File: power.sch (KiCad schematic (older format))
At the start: 28 parts, among them J1 TYPE-C-31-M-12, U4 BQ27441DRZR-G1A, U5 MCP73831-2-OT, U6 LC05111C02MTTTG, U7 TLV75733PDBV

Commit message: Did stuff
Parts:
- C5, C6, C7: footprint (none) -> Capacitor_SMD:C_0603_1608Metric_Pad1.05x0.95mm_HandSolder
- R16, R17: footprint (none) -> Resistor_SMD:R_0603_1608Metric_Pad1.05x0.95mm_HandSolder
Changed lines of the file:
@@
 	2675 3250 2375 3250
 Wire Wire Line
-	2675 3300 2675 3250
+	4075 3300 4075 3250
 $Comp
 L power:GND #PWR?
 U 1 1 5F83C52A
-P 2675 3300
+P 4075 3300
 AR Path="/5E707A75/5F83C52A" Ref="#PWR?"  Part="1"
 AR Path="/5F83C52A" Ref="#PWR?"  Part="1"
 AR Path="/5F797DCE/5F83C52A" Ref="#PWR09"  Part="1"
-F 0 "#PWR09" H 2675 3050 50  0001 C CNN
-F 1 "GND" H 2680 3127 50  0000 C CNN
-F 2 "" H 2675 3300 50  0001 C CNN
-F 3 "" H 2675 3300 50  0001 C CNN
-	1    2675 3300
+F 0 "#PWR09" H 4075 3050 50  0001 C CNN
+F 1 "GND" H 4080 3127 50  0000 C CNN
+F 2 "" H 4075 3300 50  0001 C CNN
+F 3 "" H 4075 3300 50  0001 C CNN
+	1    4075 3300
 	1    0    0    -1
 $EndComp
@@
 F 0 "R17" H 4234 4521 50  0000 L CNN
 F 1 "1K" H 4234 4430 50  0000 L CNN
-F 2 "" H 4175 4475 50  0001 C CNN
+F 2 "Resistor_SMD:R_0603_1608Metric_Pad1.05x0.95mm_HandSolder" H 4175 4475 50  0001 C CNN
 F 3 "~" H 4175 4475 50  0001 C CNN
 	1    4175 4475
@@
 F 0 "R16" H 3617 3954 50  0000 R CNN
 F 1 "680R" H 3617 4045 50  0000 R CNN
-F 2 "" H 3675 4000 50  0001 C CNN
+F 2 "Resistor_SMD:R_0603_1608Metric_Pad1.05x0.95mm_HandSolder" H 3675 4000 50  0001 C CNN
 F 3 "~" H 3675 4000 50  0001 C CNN
 	1    3675 4000
@@
 F 0 "C6" H 2875 4325 50  0000 R CNN
 F 1 "100nF" H 3000 4425 50  0000 R CNN
-F 2 "" H 2750 4525 50  0001 C CNN
+F 2 "Capacitor_SMD:C_0603_1608Metric_Pad1.05x0.95mm_HandSolder" H 2750 4525 50  0001 C CNN
 F 3 "~" H 2750 4525 50  0001 C CNN
 	1    2750 4525
@@
 F 0 "C7" H 3025 4600 50  0000 R CNN
 F 1 "100nF" H 3050 4675 50  0000 R CNN
-F 2 "" H 3075 4525 50  0001 C CNN
+F 2 "Capacitor_SMD:C_0603_1608Metric_Pad1.05x0.95mm_HandSolder" H 3075 4525 50  0001 C CNN
 F 3 "~" H 3075 4525 50  0001 C CNN
 	1    3075 4525
@@
 F 0 "C5" H 4375 4475 50  0000 R CNN
 F 1 "100nF" H 4450 4550 50  0000 R CNN
-F 2 "" H 4450 4450 50  0001 C CNN
+F 2 "Capacitor_SMD:C_0603_1608Metric_Pad1.05x0.95mm_HandSolder" H 4450 4450 50  0001 C CNN
 F 3 "~" H 4450 4450 50  0001 C CNN
 	1    4450 4450
@@
 Replace with LM66100
 Wire Notes Line
-	5725 3900 5625 3900
-Wire Notes Line
-	5625 3900 5625 4100
-Wire Notes Line
-	5625 4100 5725 4100
+	5375 3900 5375 4100
+Wire Notes Line
+	5375 4100 5725 4100
 Wire Notes Line
 	5725 4100 5725 3825
 Wire Notes Line
 	5725 3825 6575 3825
+Wire Notes Line
+	5375 3900 5725 3900
 $EndSCHEMATC

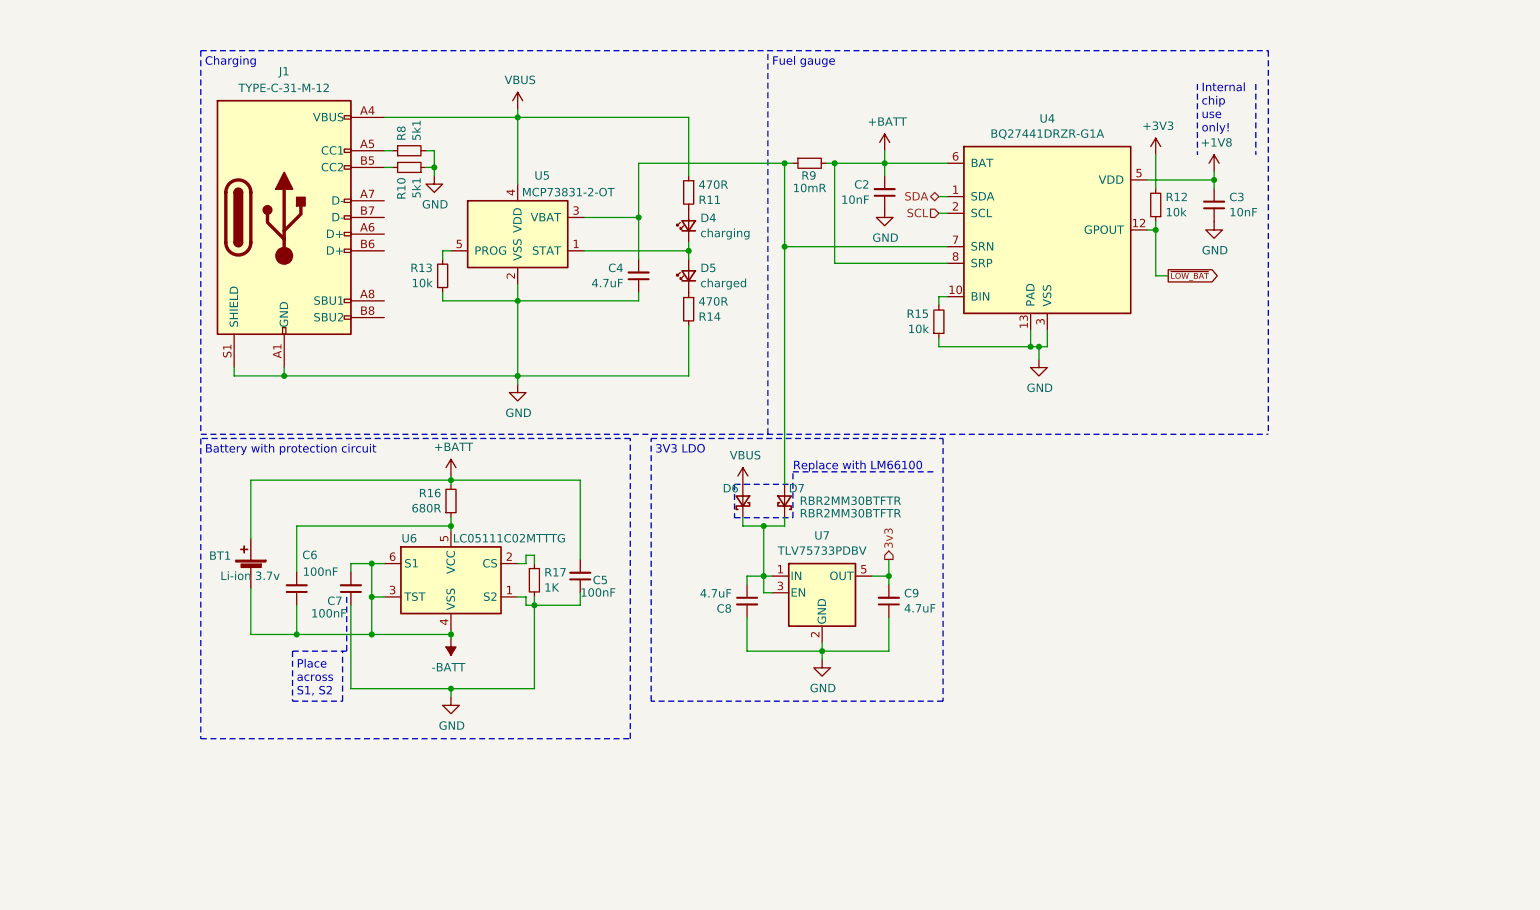
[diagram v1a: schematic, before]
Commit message: Redesigned to small-stick formfactor
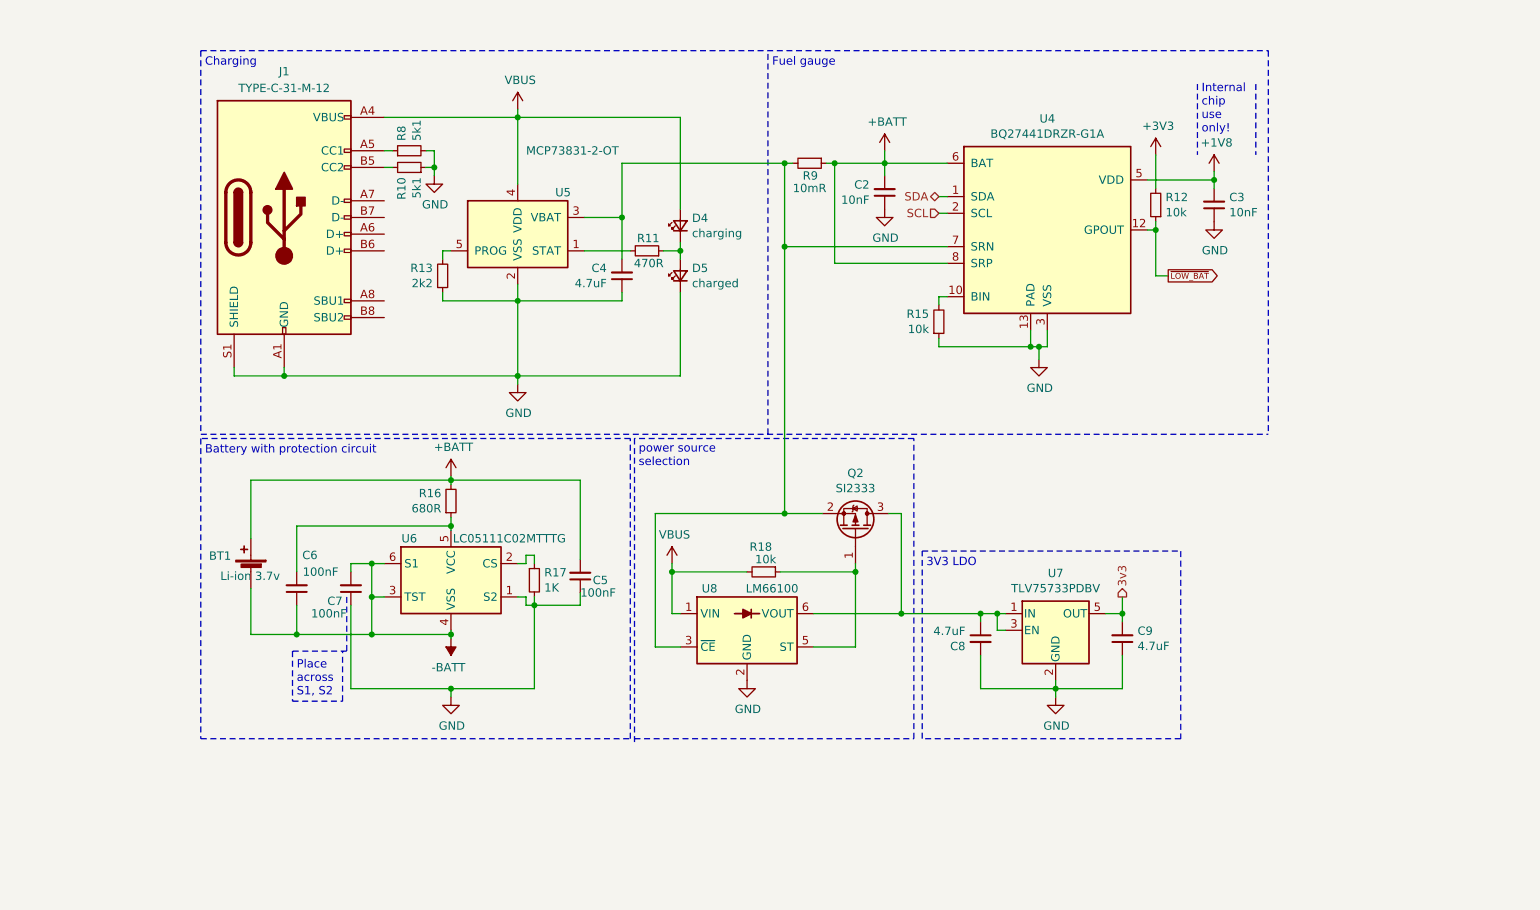
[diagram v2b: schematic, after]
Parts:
- removed D6, D7: RBR2MM30BTFTR, Diode_SMD:D_SOD-123F, symbol Device:D_Schottky_Small
- removed R14: 470R, Resistor_SMD:R_0603_1608Metric_Pad1.05x0.95mm_HandSolder, symbol Device:R_Small
- added Q2: SI2333, Package_TO_SOT_SMD:SOT-23, symbol Device:Q_PMOS_GSD
- added R18: 10k, Resistor_SMD:R_0603_1608Metric_Pad1.05x0.95mm_HandSolder, symbol Device:R_Small
- added U8: LM66100, Package_TO_SOT_SMD:SOT-363_SC-70-6, symbol Analog_Switch:LM66100
- C2, C3: footprint Capacitor_SMD:C_0603_1608Metric_Pad1.05x0.95mm_HandSolder -> Capacitor_SMD:C_0805_2012Metric_Pad1.15x1.40mm_HandSolder
- R13: value 10k -> 2k2
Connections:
- net +BATT: now also R9.1; no longer R9.2
- net GND: now also D5.1 (K), U8.2 (GND)
- net VBUS: now also D4.2 (A), R18.2, U8.1 (VIN); no longer R11.1
- net at D4.1 (K), D5.2 (A): now also R11.1; no longer U5.1 (STAT)
- net at C4.2, U4.7 (SRN), U5.3 (VBAT): now also R9.2, Q2.2 (S), U8.3 (~CE); no longer R9.1
- net at R11.2: now also U5.1 (STAT); no longer D4.2 (A)
- net at C8.1, U7.1 (IN), U7.3 (EN): now also Q2.3 (D), U8.6 (VOUT)
- new net: Q2.1 (G), R18.1, U8.5 (ST)
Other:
- note added: "power source \nselection"
- note removed: "Replace with LM66100"
- moved on the sheet: C4, C8, C9, D4, D5, R11, U7

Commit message: Added alternative fuel gauge to PCB
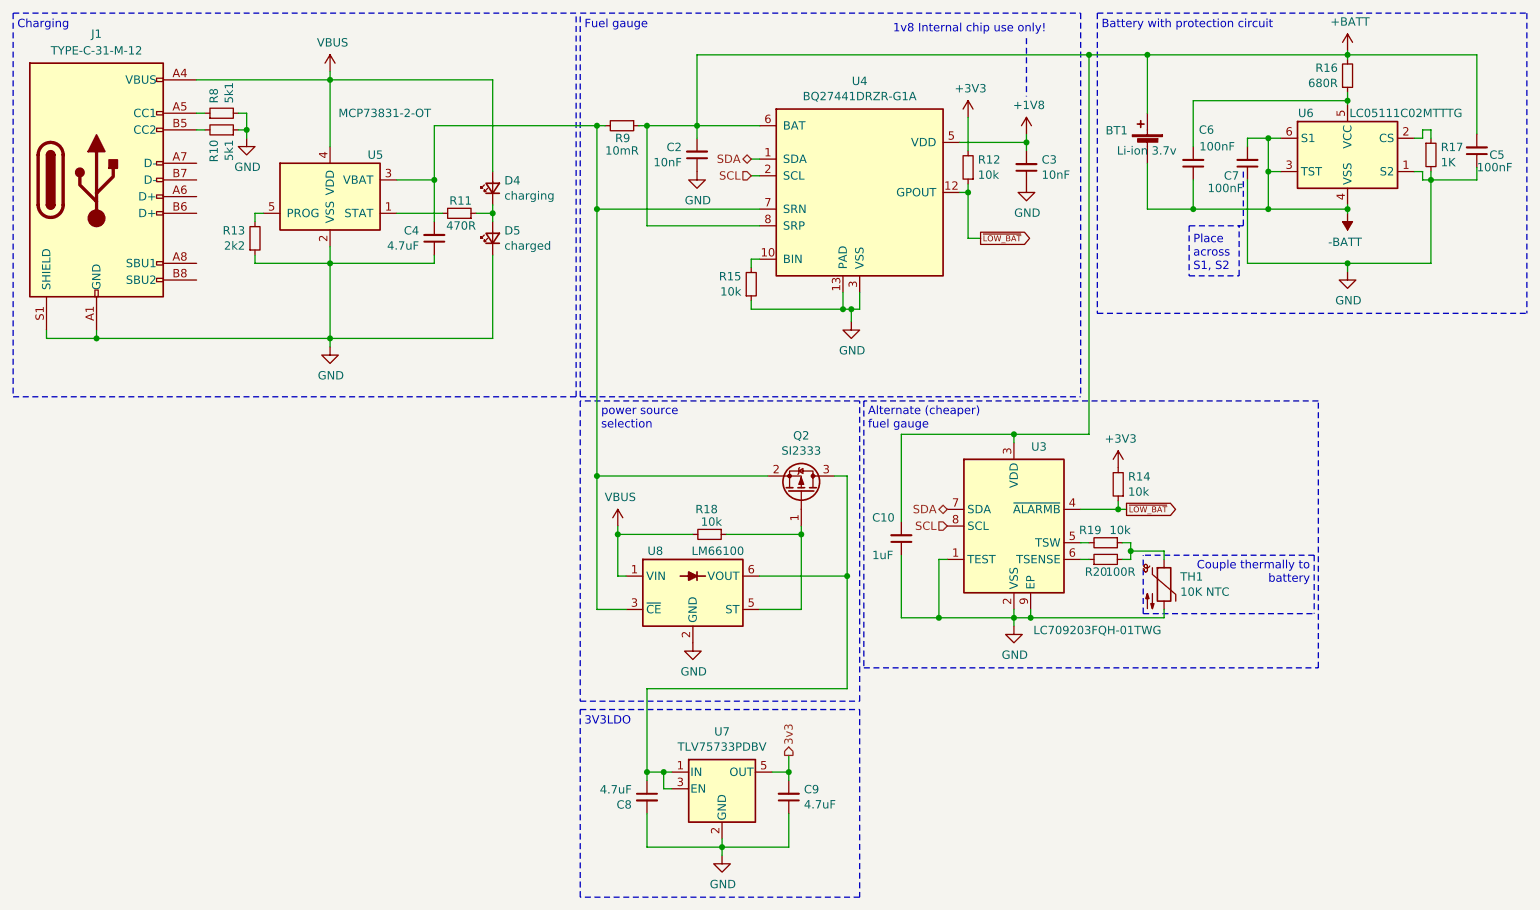
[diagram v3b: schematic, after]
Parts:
- added C10: 1uF, Capacitor_SMD:C_0603_1608Metric_Pad1.05x0.95mm_HandSolder, symbol Device:C_Small
- added R14, R19: 10k, Resistor_SMD:R_0603_1608Metric_Pad1.05x0.95mm_HandSolder, symbol Device:R_Small
- added R20: 100R, Resistor_SMD:R_0603_1608Metric_Pad1.05x0.95mm_HandSolder, symbol Device:R_Small
- added TH1: 10K NTC, symbol Device:Thermistor_NTC
- added U3: LC709203FQH-01TWG, Package_DFN_QFN:WDFN-8-1EP_4x3mm_P0.65mm_EP2.4x1.8mm, symbol Battery_Management:LC709203FQH-01TWG
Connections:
- net +3V3: now also R14.2
- net +BATT: now also C10.2, U3.3 (VDD)
- net GND: now also C10.1, TH1.2, U3.1 (TEST), U3.2 (VSS), U3.9 (EP)
- net SCL: now also U3.8 (SCL)
- net SDA: now also U3.7 (SDA)
- net ~LOW_BAT: now also R14.1, U3.4 (~ALARMB)
- new net: R19.2, U3.5 (TSW)
- new net: R20.1, U3.6 (TSENSE)
- new net: R19.1, R20.2, TH1.1
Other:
- note added: "1v8 Internal chip use only!"
- note added: "3V3LDO"
- note added: "Alternate (cheaper) \nfuel gauge"
- note added: "Couple thermally to\nbattery"
- note removed: "3V3 LDO"
- note removed: "Internal \nchip \nuse \nonly!"
- moved on the sheet: BT1, C2, C3, C4, C5, C6, C7, C8, C9, D4, D5, J1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
